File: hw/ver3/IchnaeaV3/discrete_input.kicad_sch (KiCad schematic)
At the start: 2 parts, among them U14 74HC165, U16 74HC165

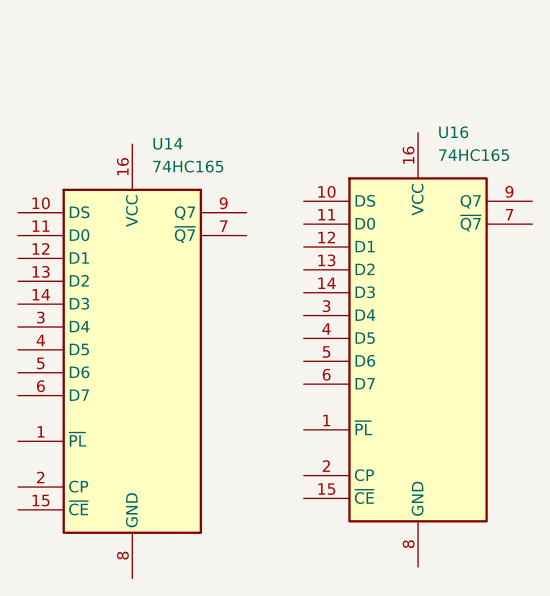
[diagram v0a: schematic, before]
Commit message: Experiment with a new power stage layout
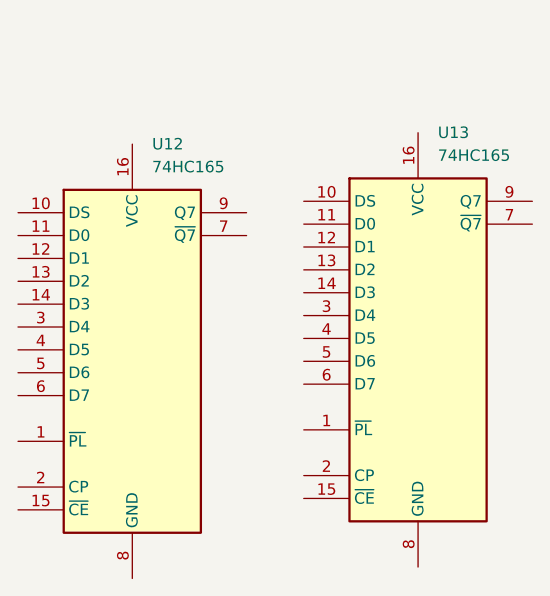
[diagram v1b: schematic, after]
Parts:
- renumbered U14 to U12, U16 to U13
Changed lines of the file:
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@@
 		(dnp no)
 		(fields_autoplaced yes)
-		(property "Reference" "U14"
+		(property "Reference" "U12"
 			(at 113.9541 63.5 0)
 			(effects
@@
 			(project "IchnaeaV3"
 				(path "/93408532-1ffa-463d-873c-16289d2b7987/f8cdf9d7-add1-4ff8-8430-918a71e3d1f9/34bfa573-b03d-46a9-b87f-fd8daed6e538"
-					(reference "U14")
+					(reference "U12")
 					(unit 1)
 				)
@@
 		(dnp no)
 		(fields_autoplaced yes)
-		(property "Reference" "U16"
+		(property "Reference" "U13"
 			(at 145.7041 62.23 0)
 			(effects
@@
 			(project "IchnaeaV3"
 				(path "/93408532-1ffa-463d-873c-16289d2b7987/f8cdf9d7-add1-4ff8-8430-918a71e3d1f9/34bfa573-b03d-46a9-b87f-fd8daed6e538"
-					(reference "U16")
+					(reference "U13")
 					(unit 1)
 				)

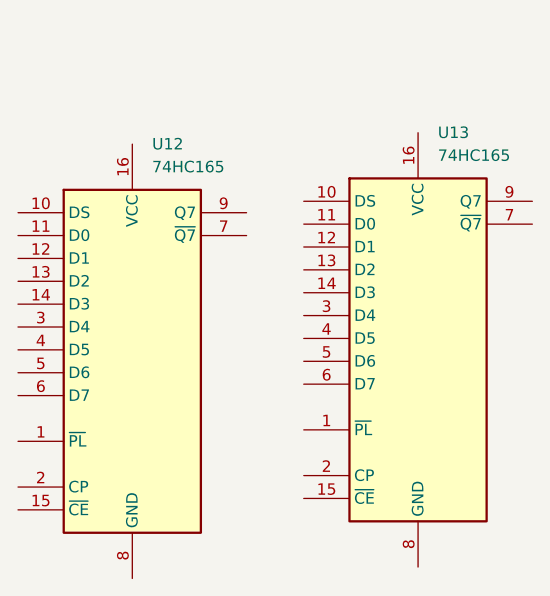
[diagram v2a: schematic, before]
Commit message: Improve more of the power stage layout
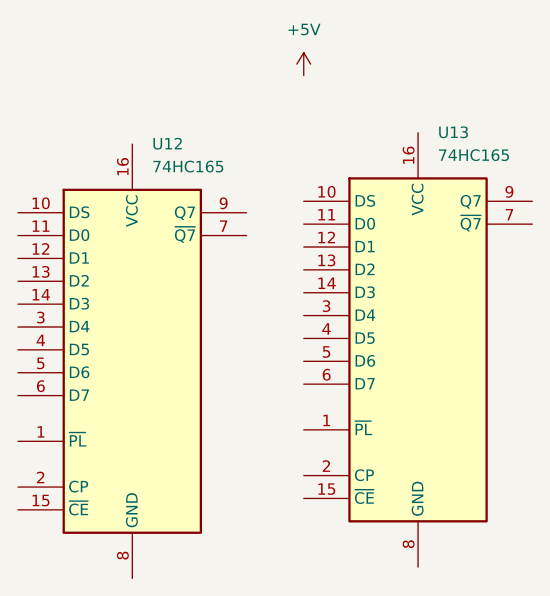
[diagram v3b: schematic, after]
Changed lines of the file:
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@@
+			)
+		)
+		(property "DigiKey" ""
+			(at 111.76 86.36 0)
+			(effects
+				(font
+					(size 1.27 1.27)
+				)
+				(hide yes)
 			)
 		)
@@
 				(path "/93408532-1ffa-463d-873c-16289d2b7987/f8cdf9d7-add1-4ff8-8430-918a71e3d1f9/34bfa573-b03d-46a9-b87f-fd8daed6e538"
 					(reference "U12")
+					(unit 1)
+				)
+			)
+		)
+	)
+	(symbol
+		(lib_id "power:+5V")
+		(at 130.81 55.88 0)
+		(unit 1)
+		(exclude_from_sim no)
+		(in_bom yes)
+		(on_board yes)
+		(dnp no)
+		(fields_autoplaced yes)
+		(property "Reference" "#PWR0132"
+			(at 130.81 59.69 0)
+			(effects
+				(font
+					(size 1.27 1.27)
+				)
+				(hide yes)
+			)
+		)
+		(property "Value" "+5V"
+			(at 130.81 50.8 0)
+			(effects
+				(font
+					(size 1.27 1.27)
+				)
+			)
+		)
+		(property "Footprint" ""
+			(at 130.81 55.88 0)
+			(effects
+				(font
+					(size 1.27 1.27)
+				)
+				(hide yes)
+			)
+		)
+		(property "Datasheet" ""
+			(at 130.81 55.88 0)
+			(effects
+				(font
+					(size 1.27 1.27)
+				)
+				(hide yes)
+			)
+		)
+		(property "Description" "Power symbol creates a global label with name \"+5V\""
+			(at 130.81 55.88 0)
+			(effects
+				(font
+					(size 1.27 1.27)
+				)
+				(hide yes)
+			)
+		)
+		(pin "1"
+		)
+		(instances
+			(project "IchnaeaV3"
+				(path "/93408532-1ffa-463d-873c-16289d2b7987/f8cdf9d7-add1-4ff8-8430-918a71e3d1f9/34bfa573-b03d-46a9-b87f-fd8daed6e538"
+					(reference "#PWR0132")
 					(unit 1)
 				)
@@
 			(at 143.51 85.09 0)
 			(effects
+				(font
+					(size 1.27 1.27)
+				)
+				(hide yes)
+			)
+		)
+		(property "DigiKey" ""
+			(at 143.51 85.09 0)
+			(effects
